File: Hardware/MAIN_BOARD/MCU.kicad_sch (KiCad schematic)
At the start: 22 parts, among them J3 Conn_01x04, J3 Conn_01x05, J9 USB_B_Micro, SW1 SW_Push, U18 CH340G, U3 STM32H750XBHx, Y1 12 Mhz

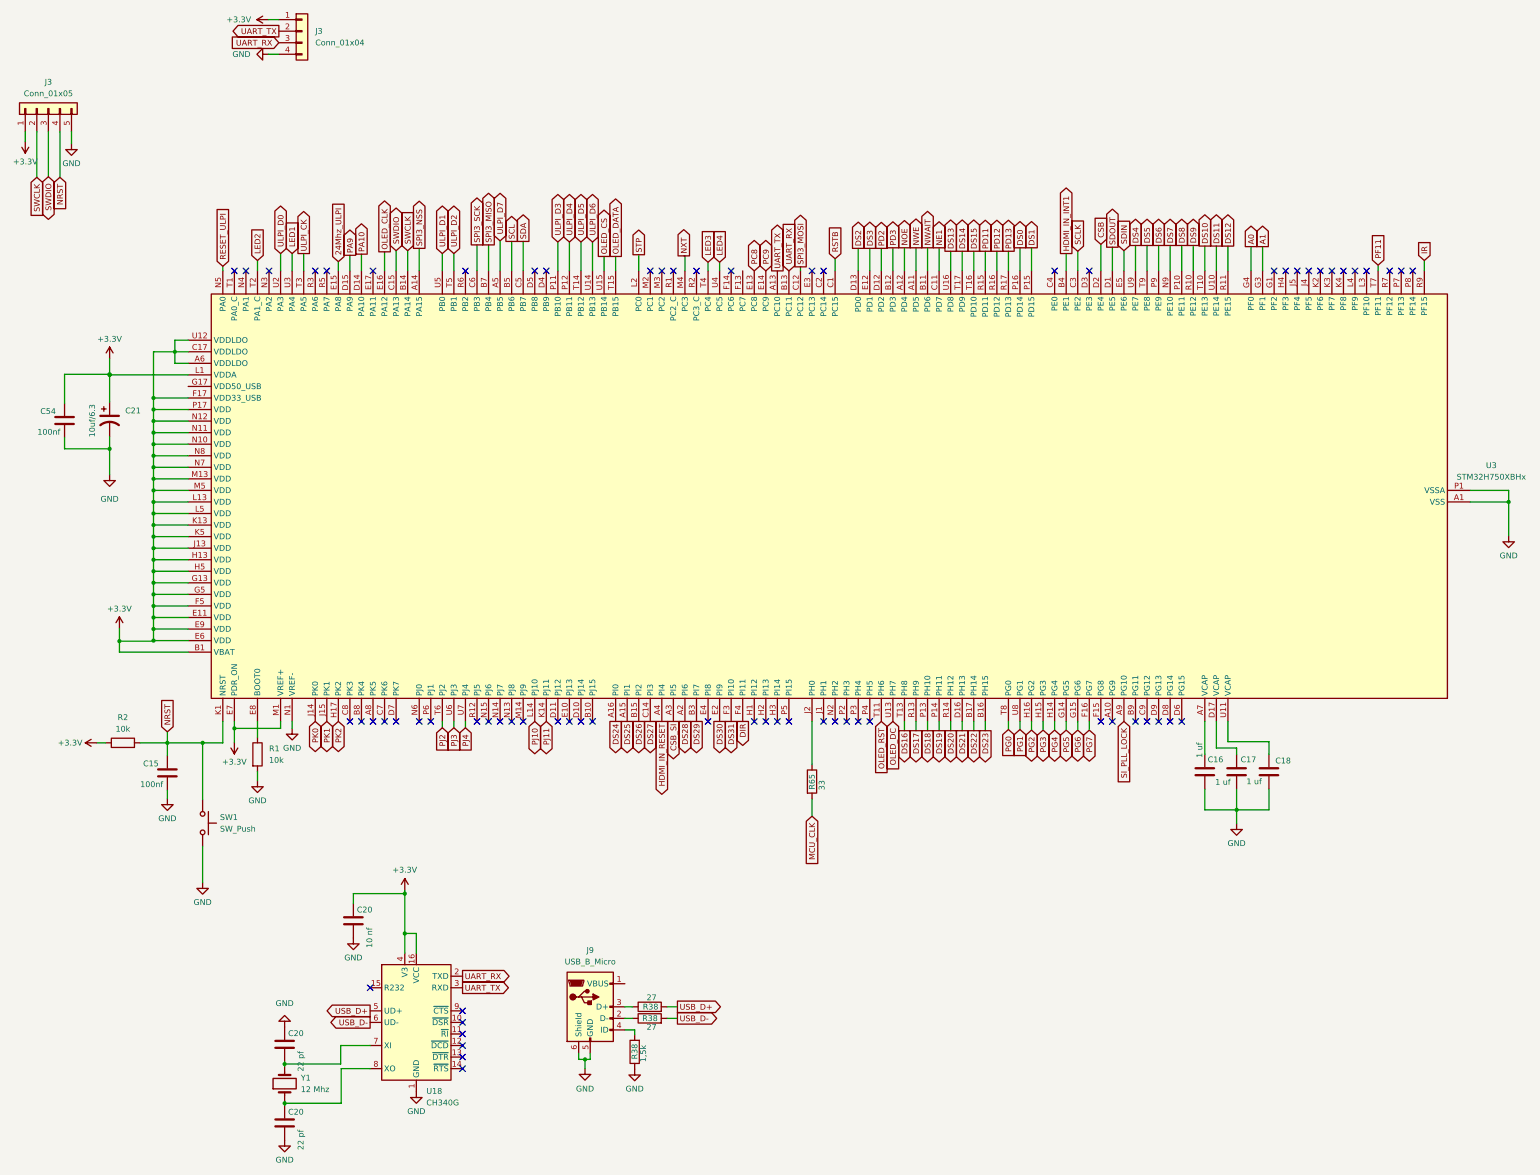
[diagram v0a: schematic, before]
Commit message: some PCB/schemtic improvements
some PCB improvements,
three additional debug LEDs,
add serial res. at data/clk line
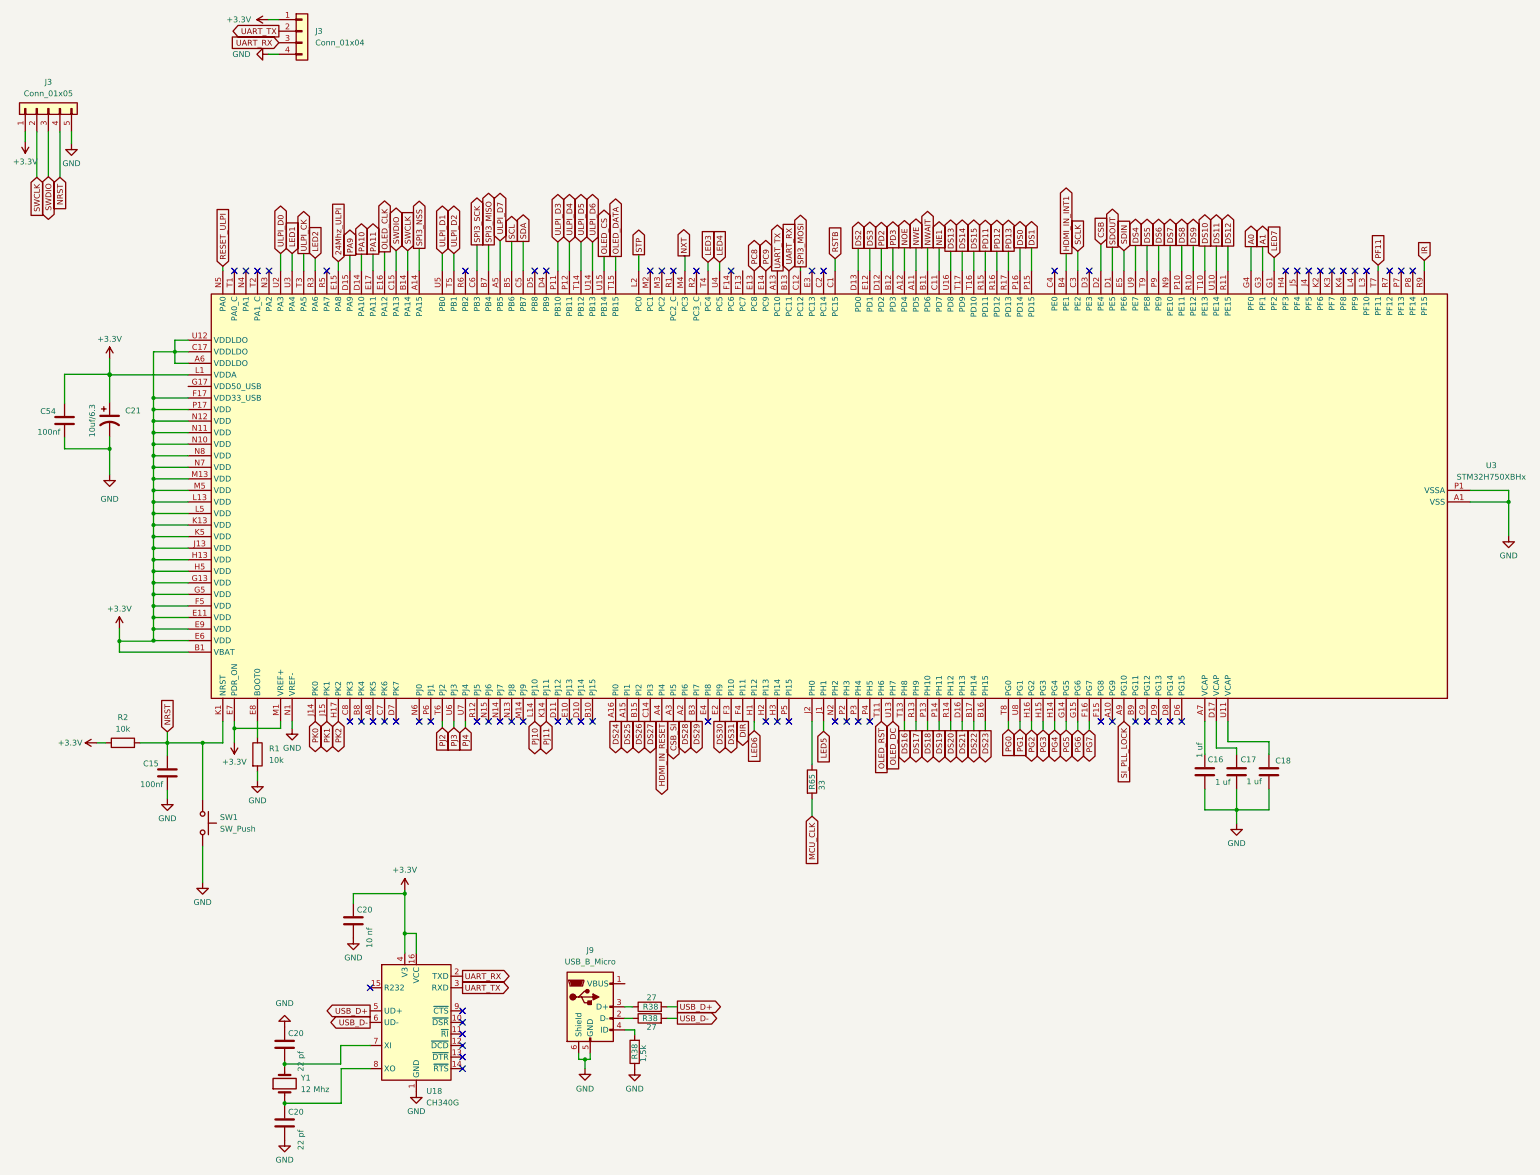
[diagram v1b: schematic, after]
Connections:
- net LED2: now also U3.R3 (PA6); no longer U3.T2 (PA1_C)
- net PA11: now reaches U3.E17 (PA11)
- net LED7: now reaches U3.G1 (PF2)
- net LED6: now reaches U3.H1 (PI12)
- net LED5: now reaches U3.J1 (PH1)
- no-connect marks 70 -> 66
